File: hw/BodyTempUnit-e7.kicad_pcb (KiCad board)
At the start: 4 copper layers, 25 x 30 mm, 28 parts, among them IC1 MAX481CUA, IC2 MEGA8-MI, U1 MAX30205MTA+21-0137I_T833-2-M, U2 LSM6DS3, U3 MCP1801T-3302I_OT

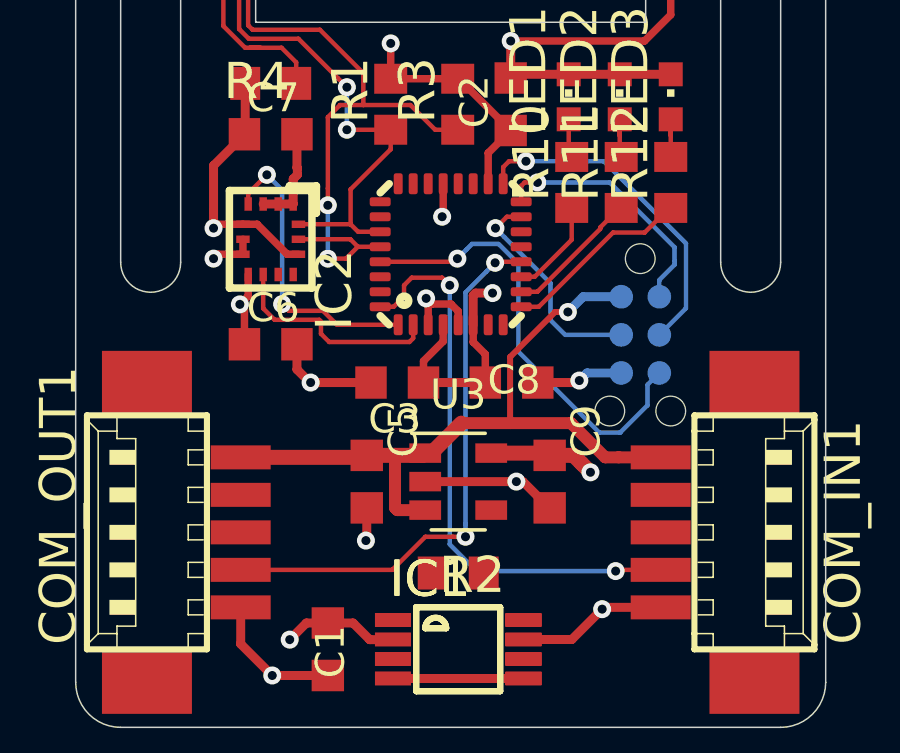
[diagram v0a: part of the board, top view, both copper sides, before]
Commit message: GND pour added to mlf footprint
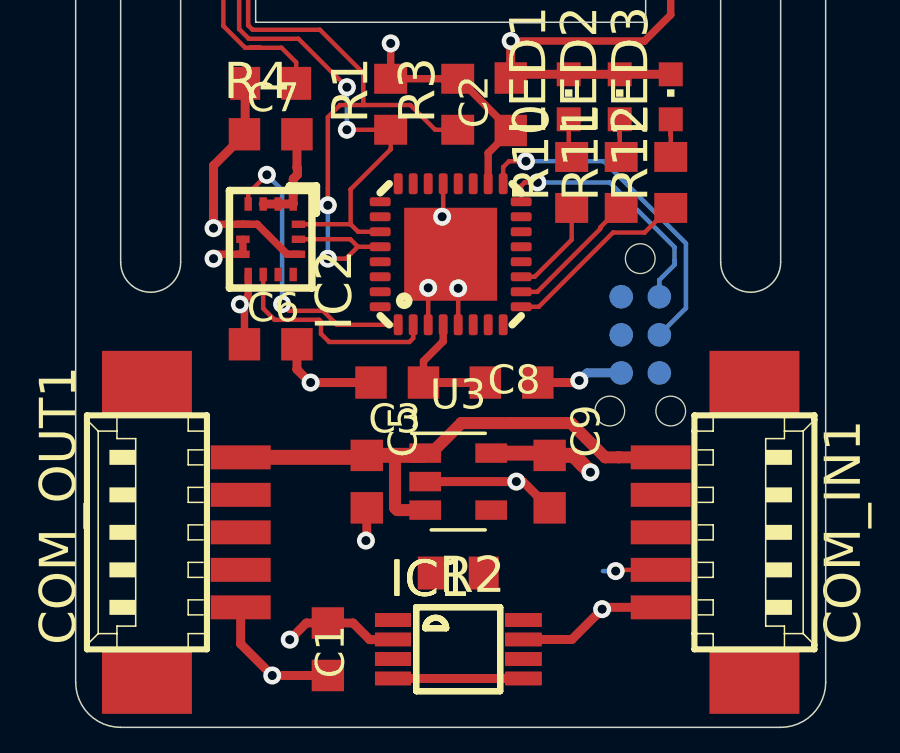
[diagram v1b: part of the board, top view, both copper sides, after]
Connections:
- COM_IN1 pad 3: /RS485_B -> /RS485_-
- COM_IN1 pad 4: /RS485_A -> /RS485_+
- COM_OUT1 pad 2: /RS485_A -> /RS485_+
- COM_OUT1 pad 3: /RS485_B -> /RS485_-
- IC1 pad 1: /RS485_B -> /RS485_-
- IC1 pad 8: /RS485_A -> /RS485_+
- IC2 pad 9: Net-(IC2-Pad9) -> /RS485_DE
- PF1 pad 2: /Vin -> VCC
- R10 pad 1: Net-(IC2-Pad11) -> Net-(IC2-Pad14)
- R11 pad 1: Net-(IC2-Pad10) -> Net-(IC2-Pad13)
- R12 pad 1: Net-(IC2-Pad9) -> Net-(IC2-Pad11)
- R2 pad 1: /RS485_B -> /RS485_-
- R2 pad 2: /RS485_A -> /RS485_+
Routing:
- net /SIG_OUT: track 18.2 -> 0.00 mm, vias 2 -> 0
- net /SIG_IN: track 19.3 -> 2.20 mm, vias 2 -> 1
- net /RST: track 15.1 -> 0.00 mm, vias 1 -> 0
- net /MOSI: track 7.40 -> 0.00 mm, vias 1 -> 0
- net /Vin: track 25.1 -> 18.3 mm, vias 1 -> 0
- net Net-(IC2-Pad9): track 6.35 -> 0.00 mm
- net Net-(IC2-Pad13): track 0.00 -> 4.52 mm
- net Net-(IC2-Pad10): track 4.52 -> 0.00 mm
- net GND: track 55.5 -> 59.5 mm, vias 16 -> 17
- net VCC: track 41.3 -> 37.6 mm, vias 7 -> 6
- net Net-(IC2-Pad14): track 0.00 -> 3.30 mm
- net Net-(IC2-Pad11): track 3.30 -> 6.35 mm

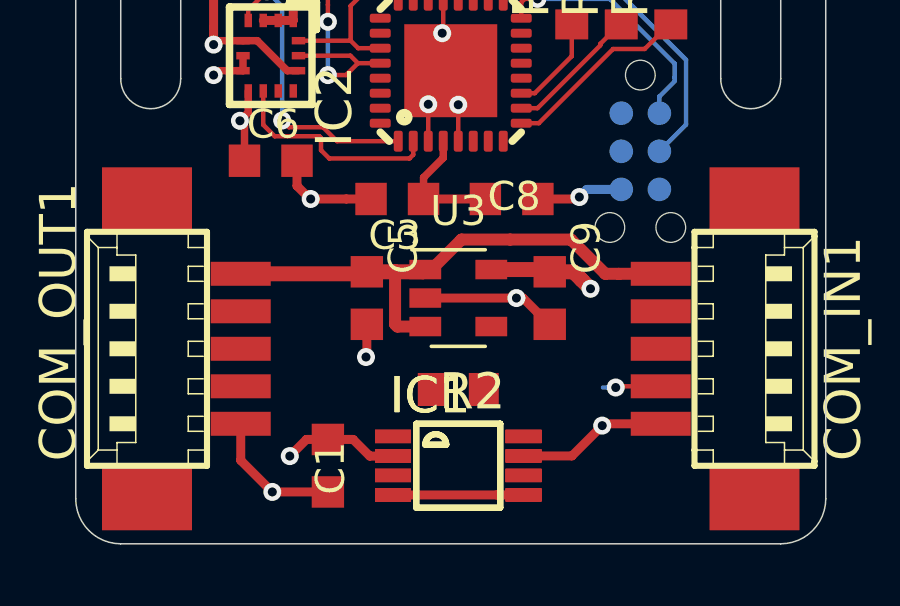
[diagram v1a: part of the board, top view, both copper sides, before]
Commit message: switched regulator with RS485
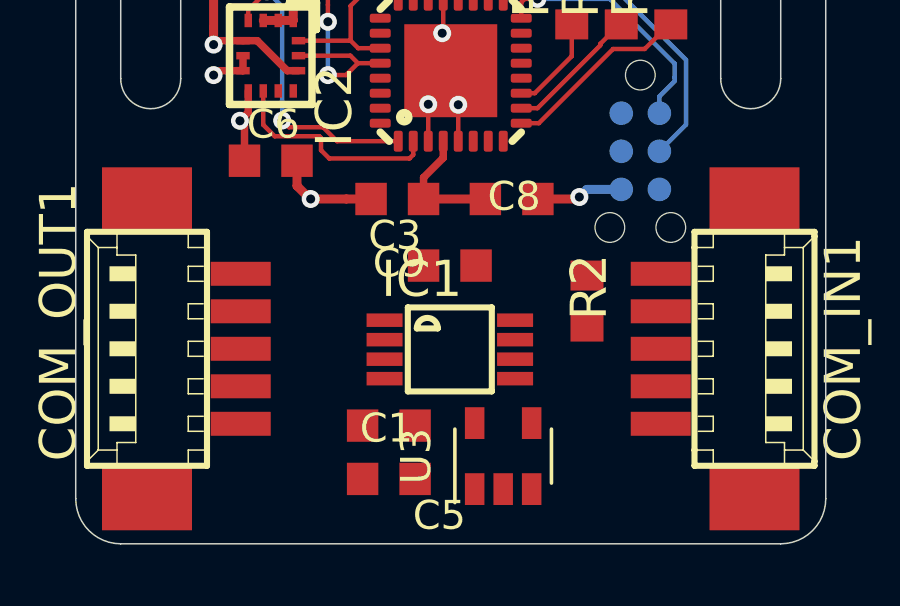
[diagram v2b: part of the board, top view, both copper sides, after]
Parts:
- removed the IC1 at (77.8, 132.4)
- moved C5 6.07 mm to (75.4, 132.8), turned to 180 degrees
- moved U3 5.48 mm to (79.2, 132.1), turned to 90 degrees
- moved R2 5.21 mm to (82.0, 126.9), turned to 90 degrees
- moved IC1 3.89 mm to (77.5, 128.5)
- moved C9 3.50 mm to (77.5, 125.7), turned to 0 degrees
- moved C1 2.43 mm to (75.4, 131.1), turned to 180 degrees
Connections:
- C5 pad 1: /Vin -> /VIN
- COM_IN1 pad 1: GND -> /VIN
- COM_IN1 pad 5: /Vin -> GND
- COM_OUT1 pad 1: /Vin -> GND
- COM_OUT1 pad 5: GND -> /VIN
- U3 pad 1: /Vin -> /VIN
- U3 pad 3: /Vin -> /VIN
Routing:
- net /Vin: track 18.3 -> 0.00 mm
- net GND: track 59.5 -> 44.9 mm, vias 17 -> 13
- net VCC: track 37.6 -> 30.1 mm, vias 6 -> 4
- net /RS485_DE: track 4.35 -> 0.00 mm
- net /SIG_IN: track 2.20 -> 0.25 mm, vias 1 -> 0
- added copper zone on In2.Cu, net /VIN
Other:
- rule trace_min: 0.0889 -> 0.15

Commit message: some rerouting
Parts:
- removed COM_IN1, COM_OUT1: 53?-05261, BodyTempUnit-e7:53261-05
- added J1: CONN_IN, Connector_Molex:Molex_PicoBlade_53261-0571_1x05-1MP_P1.25mm_Horizontal, F.Cu at (67.9, 128.5)
- added J2: CONN_OUT, Connector_Molex:Molex_PicoBlade_53261-0571_1x05-1MP_P1.25mm_Horizontal, F.Cu at (87.1, 128.5)
- C4: footprint BodyTempUnit-e7:C0603K -> Capacitor_SMD:C_0402_1005Metric
- PF1: moved to F.Cu
- R4: footprint BodyTempUnit-e7:R0603 -> Resistor_SMD:R_0402_1005Metric
- moved R4 10.6 mm to (80.3, 107.7), turned to 90 degrees
- moved R2 9.69 mm to (72.4, 127.9)
- moved LED1 9.45 mm to (85.1, 122.7), turned to 180 degrees
- moved LED3 8.85 mm to (83.4, 122.7), turned to 180 degrees
- moved LED2 8.84 mm to (81.8, 122.7), turned to 180 degrees
- moved PF1 7.43 mm to (84.2, 114.5)
- moved C4 6.30 mm to (74.7, 107.6)
- moved R10 5.04 mm to (85.6, 119.9), turned to 270 degrees
- moved C9 4.43 mm to (81.9, 125.9), turned to 90 degrees
- moved R12 3.14 mm to (84.0, 119.9), turned to 270 degrees
- moved R11 3.14 mm to (82.3, 119.9), turned to 270 degrees
- moved IC1 1.82 mm to (77.5, 126.7), turned to 90 degrees
- moved C8 0.33 mm to (79.2, 123.5)
- moved U1 0.13 mm to (77.5, 107.7), turned to 90 degrees
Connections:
- IC2 pad 10: Net-(IC2-Pad10) -> /SIG_OUT
- IC2 pad 12: /SIG_OUT -> Net-(IC2-Pad12)
- R12 pad 1: Net-(IC2-Pad11) -> Net-(IC2-Pad12)
- U1 pad 5: GND -> VCC
- U1 pad 6: GND -> VCC
- U1 pad 7: GND -> VCC
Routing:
- net GND: track 44.9 -> 12.6 mm, vias 13 -> 11
- net /RS485_-: track 0.00 -> 18.0 mm, vias 0 -> 2
- net /RS485_+: track 0.00 -> 16.4 mm
- net VCC: track 30.1 -> 15.6 mm, vias 4 -> 1
- net /RS485_RO: track 0.00 -> 13.7 mm, vias 0 -> 4
- net /SIG_IN: track 0.25 -> 13.7 mm, vias 0 -> 2
- net /SIG_OUT: track 0.00 -> 12.9 mm, vias 0 -> 2
- net /RST: track 0.00 -> 12.2 mm, vias 0 -> 2
- net /MOSI: track 0.00 -> 10.2 mm, vias 0 -> 2
- net /RS485_DE: track 0.00 -> 9.52 mm, vias 0 -> 2
- net /U1_OS: track 13.6 -> 5.36 mm, vias 2 -> 0
- net /RS485_DI: track 0.00 -> 8.05 mm, vias 0 -> 2
- net /SCL: track 29.5 -> 21.8 mm
- net /SDA: track 25.0 -> 18.6 mm
- net Net-(IC2-Pad11): track 6.35 -> 0.00 mm
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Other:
- outline, holes or cut-outs redrawn
- net class Default: trace_width 0.25 -> 0.2
- rule via_min_drill: 0.3 -> 0.2
- rule via_min_size: 0.4 -> 0.45

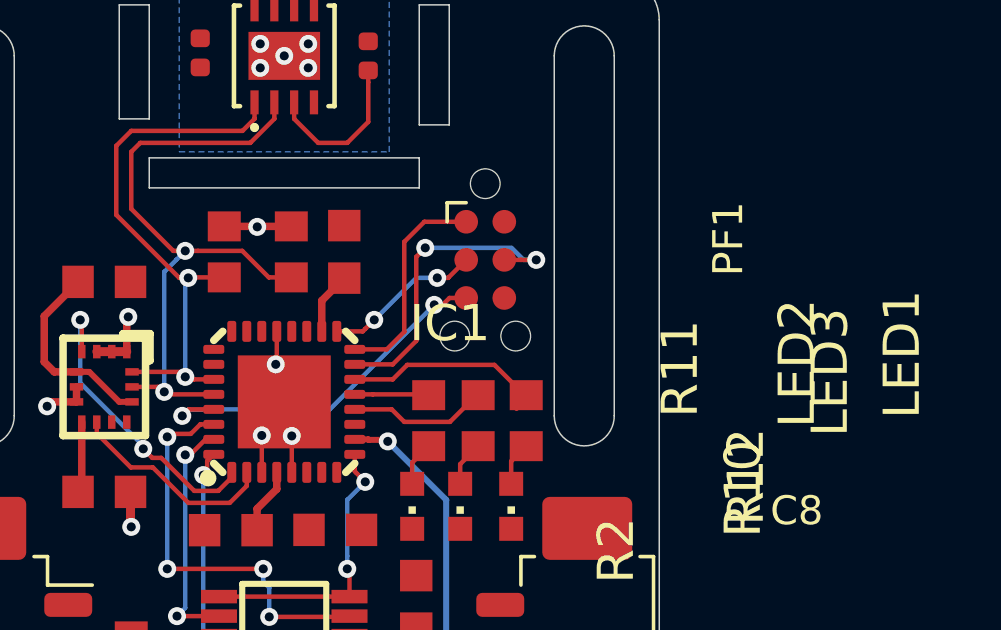
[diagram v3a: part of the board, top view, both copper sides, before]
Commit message: Reroute ISP
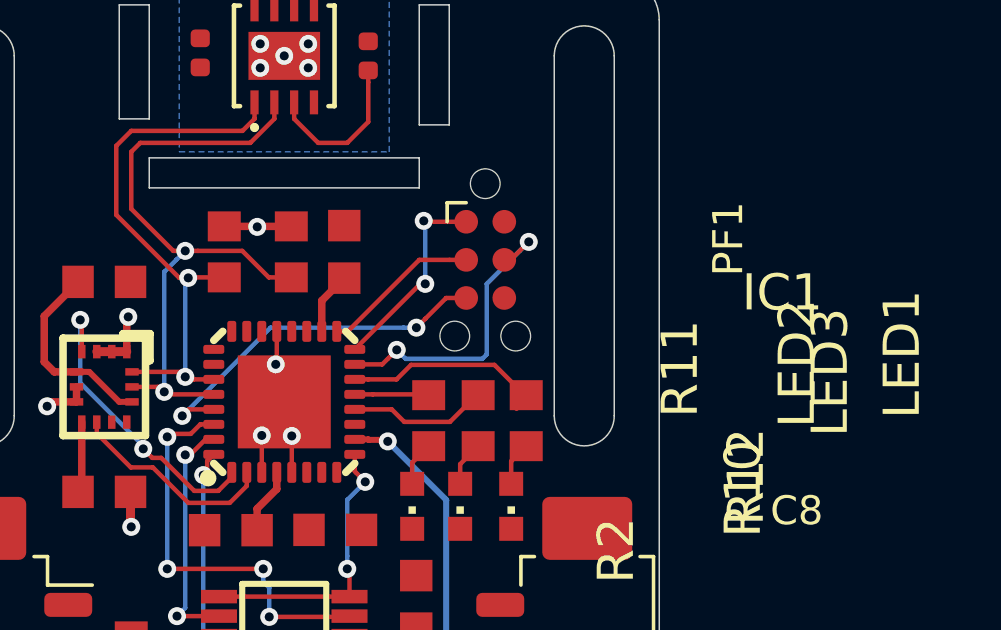
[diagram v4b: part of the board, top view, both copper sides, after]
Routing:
- net /MISO: track 7.23 -> 6.80 mm, vias 0 -> 2
- net /SCK: vias 2 -> 0
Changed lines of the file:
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@@
     (thickness 1.6)
     (drawings 29)
-    (tracks 261)
+    (tracks 262)
     (zones 0)
     (modules 27)
@@
   )
   (setup
-    (last_trace_width 0.25)
+    (last_trace_width 0.15)
     (user_trace_width 0.15)
     (user_trace_width 0.2)
@@
     (at 77.5 126.7 90)
     (descr "<b>micro MAX Package</b>")
-    (fp_text reference IC1 (at 9.376 6.87) (layer F.SilkS)
+    (fp_text reference IC1 (at 10.4 17.95) (layer F.SilkS)
       (effects (font (size 1.2065 1.2065) (thickness 0.1016)) (justify right bottom))
     )
@@
   (segment (start 75.7511 121.7489) (end 75.3 122.2) (width 0.15) (layer Top) (net 14))
   (segment (start 85.245 119.4164) (end 85.245 119.4664) (width 0.15) (layer Top) (net 22))
+  (segment (start 80.3011 118.4836) (end 79.8511 118.4836) (width 0.15) (layer Top) (net 22))
+  (segment (start 81.727007 118) (end 81.243407 118.4836) (width 0.15) (layer Top) (net 22))
+  (segment (start 84.506 118) (end 81.727007 118) (width 0.15) (layer Top) (net 22))
   (segment (start 85.516 119.01) (end 84.506 118) (width 0.15) (layer Top) (net 22))
+  (segment (start 81.243407 118.4836) (end 80.3011 118.4836) (width 0.15) (layer Top) (net 22))
   (segment (start 85.566 119.01) (end 85.516 119.01) (width 0.15) (layer Top) (net 22))
-  (segment (start 84.506 118) (end 81.6 118) (width 0.15) (layer Top) (net 22))
-  (segment (start 81.6 118) (end 81.1164 118.4836) (width 0.15) (layer Top) (net 22))
-  (segment (start 81.1164 118.4836) (end 79.8511 118.4836) (width 0.15) (layer Top) (net 22))
   (segment (start 82.2886 118.9836) (end 82.315 119.01) (width 0.15) (layer Top) (net 23))
   (segment (start 80.4511 118.9836) (end 82.2886 118.9836) (width 0.15) (layer Top) (net 23))
@@
   (segment (start 83.364 121.31) (end 83.964 120.71) (width 0.15) (layer Top) (net 29))
   (segment (start 83.364 121.965) (end 83.364 121.31) (width 0.15) (layer Top) (net 29))
-  (segment (start 83.008225 115.77) (end 82.778225 116) (width 0.15) (layer Top) (net 31))
-  (segment (start 83.565 115.77) (end 83.008225 115.77) (width 0.15) (layer Top) (net 31))
-  (via (at 82.5 116) (size 0.6) (drill 0.3) (layers Top Bottom) (net 31))
-  (segment (start 82.778225 116) (end 82.5 116) (width 0.15) (layer Top) (net 31))
   (via (at 74.100052 119.7) (size 0.6) (drill 0.3) (layers Top Bottom) (net 31))
   (segment (start 75.1511 119.4836) (end 74.316452 119.4836) (width 0.15) (layer Top) (net 31))
   (segment (start 74.316452 119.4836) (end 74.100052 119.7) (width 0.15) (layer Top) (net 31))
-  (segment (start 74.316452 119.4836) (end 74.100052 119.7) (width 0.15) (layer Bottom) (net 31))
-  (segment (start 82.5 116) (end 79.0164 119.4836) (width 0.15) (layer Bottom) (net 31))
-  (segment (start 79.0164 119.4836) (end 74.316452 119.4836) (width 0.15) (layer Bottom) (net 31))
-  (via (at 82.6 115.1) (size 0.6) (drill 0.3) (layers Top Bottom) (net 32))
-  (via (at 80.499968 116.499968) (size 0.6) (drill 0.3) (layers Top Bottom) (net 32))
-  (segment (start 80.116336 116.8836) (end 80.199969 116.799967) (width 0.15) (layer Top) (net 32))
-  (segment (start 80.199969 116.799967) (end 80.499968 116.499968) (width 0.15) (layer Top) (net 32))
-  (segment (start 79.2511 116.8836) (end 80.116336 116.8836) (width 0.15) (layer Top) (net 32))
-  (segment (start 83.565 114.5) (end 82.965 115.1) (width 0.15) (layer Top) (net 32))
-  (segment (start 82.965 115.1) (end 82.6 115.1) (width 0.15) (layer Top) (net 32))
-  (segment (start 80.500032 116.499968) (end 80.499968 116.499968) (width 0.15) (layer Bottom) (net 32))
-  (segment (start 82.6 115.1) (end 81.9 115.1) (width 0.15) (layer Bottom) (net 32))
-  (segment (start 81.9 115.1) (end 80.500032 116.499968) (width 0.15) (layer Bottom) (net 32))
-  (segment (start 80.9164 117.4836) (end 79.8511 117.4836) (width 0.15) (layer Top) (net 33))
-  (segment (start 81.5 116.9) (end 80.9164 117.4836) (width 0.15) (layer Top) (net 33))
-  (segment (start 81.5 113.9) (end 81.5 116.9) (width 0.15) (layer Top) (net 33))
-  (segment (start 83.565 113.23) (end 82.17 113.23) (width 0.15) (layer Top) (net 33))
-  (segment (start 82.17 113.23) (end 81.5 113.9) (width 0.15) (layer Top) (net 33))
-  (via (at 85.9 114.5) (size 0.6) (drill 0.3) (layers Top Bottom) (net 34))
-  (segment (start 85.391775 114.5) (end 85.9 114.5) (width 0.15) (layer Top) (net 34))
-  (segment (start 84.835 114.5) (end 85.391775 114.5) (width 0.15) (layer Top) (net 34))
-  (segment (start 85.475736 114.5) (end 85.075736 114.1) (width 0.15) (layer Bottom) (net 34))
-  (segment (start 85.9 114.5) (end 85.475736 114.5) (width 0.15) (layer Bottom) (net 34))
-  (segment (start 85.075736 114.1) (end 82.5 114.1) (width 0.15) (layer Bottom) (net 34))
-  (via (at 82.2 114.1) (size 0.6) (drill 0.3) (layers Top Bottom) (net 34))
-  (segment (start 81.9 114.4) (end 82.2 114.1) (width 0.15) (layer Top) (net 34))
-  (segment (start 81.9 117.2) (end 81.9 114.4) (width 0.15) (layer Top) (net 34))
-  (segment (start 79.8511 117.9836) (end 81.1164 117.9836) (width 0.15) (layer Top) (net 34))
-  (segment (start 81.1164 117.9836) (end 81.9 117.2) (width 0.15) (layer Top) (net 34))
+  (segment (start 82.205582 116.460364) (end 81.905583 116.760363) (width 0.15) (layer Top) (net 31))
+  (segment (start 82.895946 115.77) (end 82.205582 116.460364) (width 0.15) (layer Top) (net 31))
+  (via (at 81.905583 116.760363) (size 0.6) (drill 0.3) (layers Top Bottom) (net 31))
+  (segment (start 83.565 115.77) (end 82.895946 115.77) (width 0.15) (layer Top) (net 31))
+  (segment (start 81.481319 116.760363) (end 81.905583 116.760363) (width 0.15) (layer Bottom) (net 31))
+  (segment (start 74.100052 119.7) (end 77.039689 116.760363) (width 0.15) (layer Bottom) (net 31))
+  (segment (start 77.039689 116.760363) (end 81.481319 116.760363) (width 0.15) (layer Bottom) (net 31))
+  (segment (start 83.008225 114.5) (end 83.565 114.5) (width 0.15) (layer Top) (net 32))
+  (segment (start 82 114.5) (end 83.008225 114.5) (width 0.15) (layer Top) (net 32))
+  (segment (start 79.2511 116.8836) (end 79.6164 116.8836) (width 0.15) (layer Top) (net 32))
+  (segment (start 79.6164 116.8836) (end 82 114.5) (width 0.15) (layer Top) (net 32))
+  (segment (start 79.8511 117.4836) (end 82.0347 115.3) (width 0.15) (layer Top) (net 33))
+  (via (at 82.2 115.3) (size 0.6) (drill 0.3) (layers Top Bottom) (net 33))
+  (segment (start 82.0347 115.3) (end 82.2 115.3) (width 0.15) (layer Top) (net 33))
+  (via (at 82.149998 113.2) (size 0.6) (drill 0.3) (layers Top Bottom) (net 33))
+  (segment (start 82.2 115.3) (end 82.2 113.250002) (width 0.15) (layer Bottom) (net 33))
+  (segment (start 82.2 113.250002) (end 82.149998 113.2) (width 0.15) (layer Bottom) (net 33))
+  (segment (start 83.565 113.23) (end 82.179998 113.23) (width 0.15) (layer Top) (net 33))
+  (segment (start 82.179998 113.23) (end 82.149998 113.2) (width 0.15) (layer Top) (net 33))
+  (via (at 81.25 117.5) (size 0.6) (drill 0.3) (layers Top Bottom) (net 34))
+  (segment (start 80.950001 117.799999) (end 81.25 117.5) (width 0.15) (layer Top) (net 34))
+  (segment (start 79.8511 117.9836) (end 80.7664 117.9836) (width 0.15) (layer Top) (net 34))
+  (segment (start 80.7664 117.9836) (end 80.950001 117.799999) (width 0.15) (layer Top) (net 34))
+  (via (at 85.649996 113.9) (size 0.6) (drill 0.3) (layers Top Bottom) (net 34))
+  (segment (start 85.349997 114.199999) (end 85.649996 113.9) (width 0.15) (layer Bottom) (net 34))
+  (segment (start 84.25 117.65) (end 84.25 115.299996) (width 0.15) (layer Bottom) (net 34))
+  (segment (start 84.25 115.299996) (end 85.349997 114.199999) (width 0.15) (layer Bottom) (net 34))
+  (segment (start 84.100001 117.799999) (end 84.25 117.65) (width 0.15) (layer Bottom) (net 34))
+  (segment (start 81.549999 117.799999) (end 84.100001 117.799999) (width 0.15) (layer Bottom) (net 34))
+  (segment (start 81.25 117.5) (end 81.549999 117.799999) (width 0.15) (layer Bottom) (net 34))
+  (segment (start 85.649996 113.900004) (end 85.649996 113.9) (width 0.15) (layer Top) (net 34))
+  (segment (start 84.835 114.5) (end 85.05 114.5) (width 0.15) (layer Top) (net 34))
+  (segment (start 85.05 114.5) (end 85.649996 113.900004) (width 0.15) (layer Top) (net 34))
   (segment (start 72.2 127.25) (end 72.4 127.05) (width 0.175006) (layer Top) (net 35))
   (segment (start 70.3 127.25) (end 72.2 127.25) (width 0.175006) (layer Top) (net 35))

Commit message: Routing mostly done
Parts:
- moved C5 0.36 mm to (75.4, 133.2)
- moved C1 0.14 mm to (75.4, 131.2)
- moved U3 0.12 mm to (79.2, 132.2)
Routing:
- net VCC: track 15.6 -> 25.6 mm, vias 1 -> 9
- net GND: track 12.6 -> 17.4 mm, vias 11 -> 17
- net /RS485_RO: track 13.7 -> 15.4 mm
- net /RS485_DI: track 8.05 -> 8.76 mm
- net /SIG_IN: track 13.7 -> 13.1 mm
- added copper zone on F.Cu, net /VIN
- added copper zone on F.Cu, net GND
- removed copper zone on In2.Cu, net /VIN
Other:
- outline, holes or cut-outs redrawn
- net class Power: trace_width 0.5 -> 0.25

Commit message: Ready for final check
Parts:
- moved C1 1.09 mm to (76.5, 131.2)
- moved C5 1.09 mm to (76.5, 133.2)
- moved U3 1.08 mm to (80.3, 132.3)
- moved C4 0.16 mm to (74.8, 107.7)
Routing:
- net VCC: track 25.6 -> 40.8 mm, vias 9 -> 11
- net GND: track 17.4 -> 24.0 mm, vias 17 -> 28
- net /VIN: track 0.00 -> 2.23 mm
- added copper zone on F.Cu, net VCC
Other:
- outline, holes or cut-outs redrawn

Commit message: All routed, final check pending
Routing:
- net /SIG_OUT: track 12.9 -> 14.2 mm
- net GND: track 24.0 -> 23.1 mm, vias 28 -> 30
- net /SIG_IN: track 13.1 -> 13.8 mm
